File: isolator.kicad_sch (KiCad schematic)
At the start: 114 parts, among them J1 USB_C_Receptacle_USB2.0_16P, J2 USB_C_Receptacle_PowerOnly_6P, J3 USB_A, J4 USB_A, J5 USB_C_Receptacle_USB2.0_16P, J6 USB_C_Receptacle_USB2.0_16P, Q1 2N7002, T1 750313638, U1 ADuM4165, U10 TPS2553DBV, U11 TPS2553DBV, U12 TPS2553DBV, U13 TLV7041DBV, U14 TLV7041DBV, U15 NUP4202, U16 NUP4202, U17 NUP4202, U18 NUP4202, U2 NUP4202, U3 NUP4202, U4 USB2514B_Bi, U5 SN6505BDBV, U6 MIC29302WU, U7 TPS2121, U8 AP2112K-3.3, U9 TPS2553DBV, Y1 24M, Y2 24M

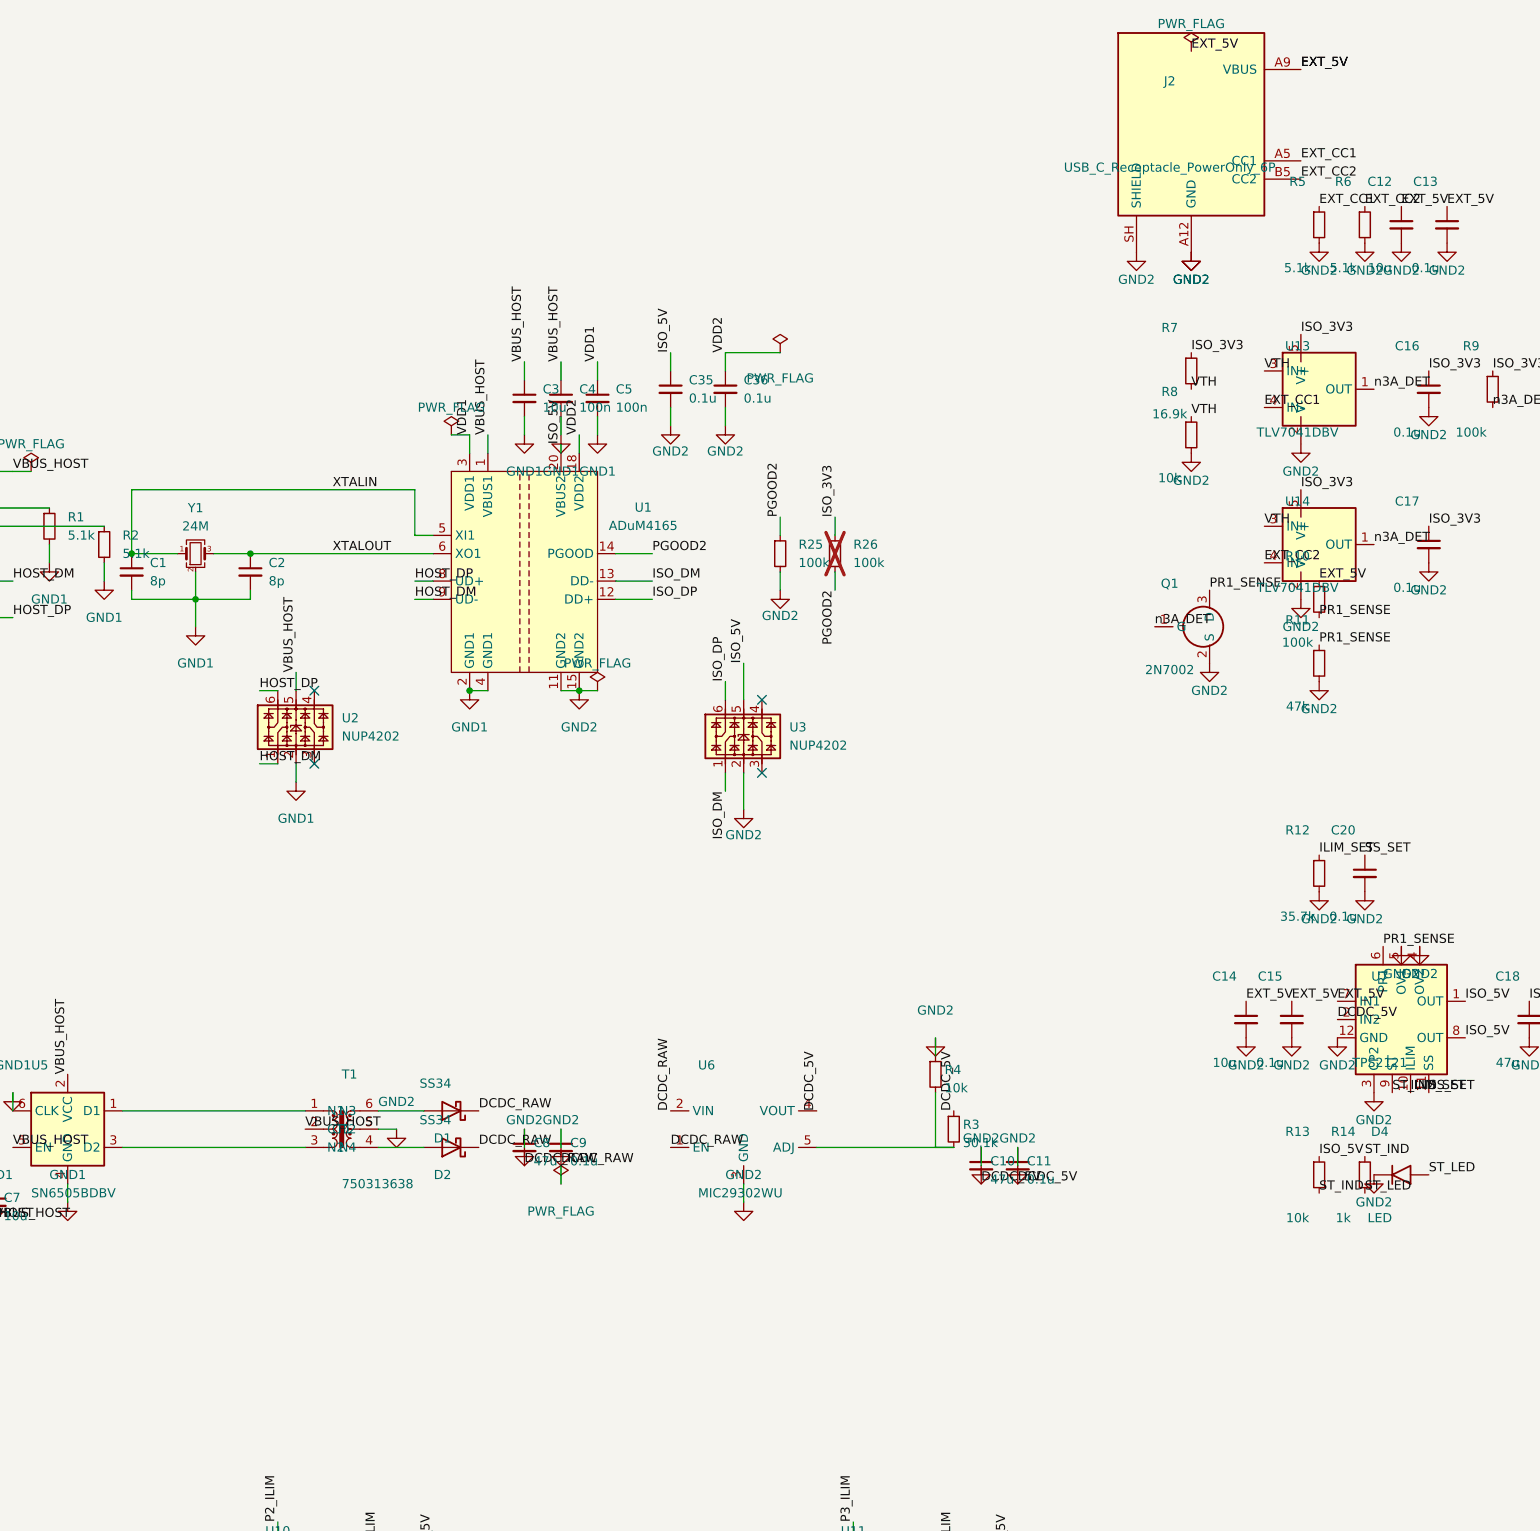
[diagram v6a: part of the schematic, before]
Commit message: feat(sch): indicators, PWR_FLAGs, stitching provision; ERC clean
Add D3 (PGOOD indicator, buffered through spare 2N7002 Q2 so the LED
never loads the shared PGOOD2 logic node) and D6 (DCDC bus-power
indicator, direct on the regulated DCDC_5V rail). Add C_stitch (1nF
2kV, DNP, in_bom no) as the sole deliberate GND1<->GND2 EMI stitching
provision besides U1, with a schematic text note. Verify the Task 4-8
PWR_FLAG sweep already covers every required rail (nothing added).
Audit no_connects: 19 total, zero stale/colliding with wires.

Reconcile lib_symbol_mismatch: fixed 5 of 11 (D_Schottky, MIC29302WU,
USB_C_Receptacle_PowerOnly_6P, LED) by restoring metadata/graphics
dropped from the cached copies vs the system library. The remaining 6
(SN6505BDBV, 2N7002 x2, TLV7041DBV x2, AP2112K-3.3, USB2514B_Bi) stay
mismatched for one-line documented reasons each: 4 are extends-vs-
flatten structural (this project's sym-lib-table only registers
isolator-lib, so caching a parent-referencing "extends" pointer would
require also caching the parent -- flattening keeps the file
self-contained, established since Task 5); 2 are the project's
intentional blank-Footprint-until-BOM-task convention (U4, U8).

ERC: 0 severity errors, exit 0. Full run: 0 errors, 7 warnings (all
justified lib_symbol_mismatch). Analyzer: ground_domains now shows
GND1 n GND2 = {U1, C_stitch}, exactly the two-domain check this task
was expected to produce.

Co-Authored-By: Claude Fable 5 <noreply@anthropic.com>
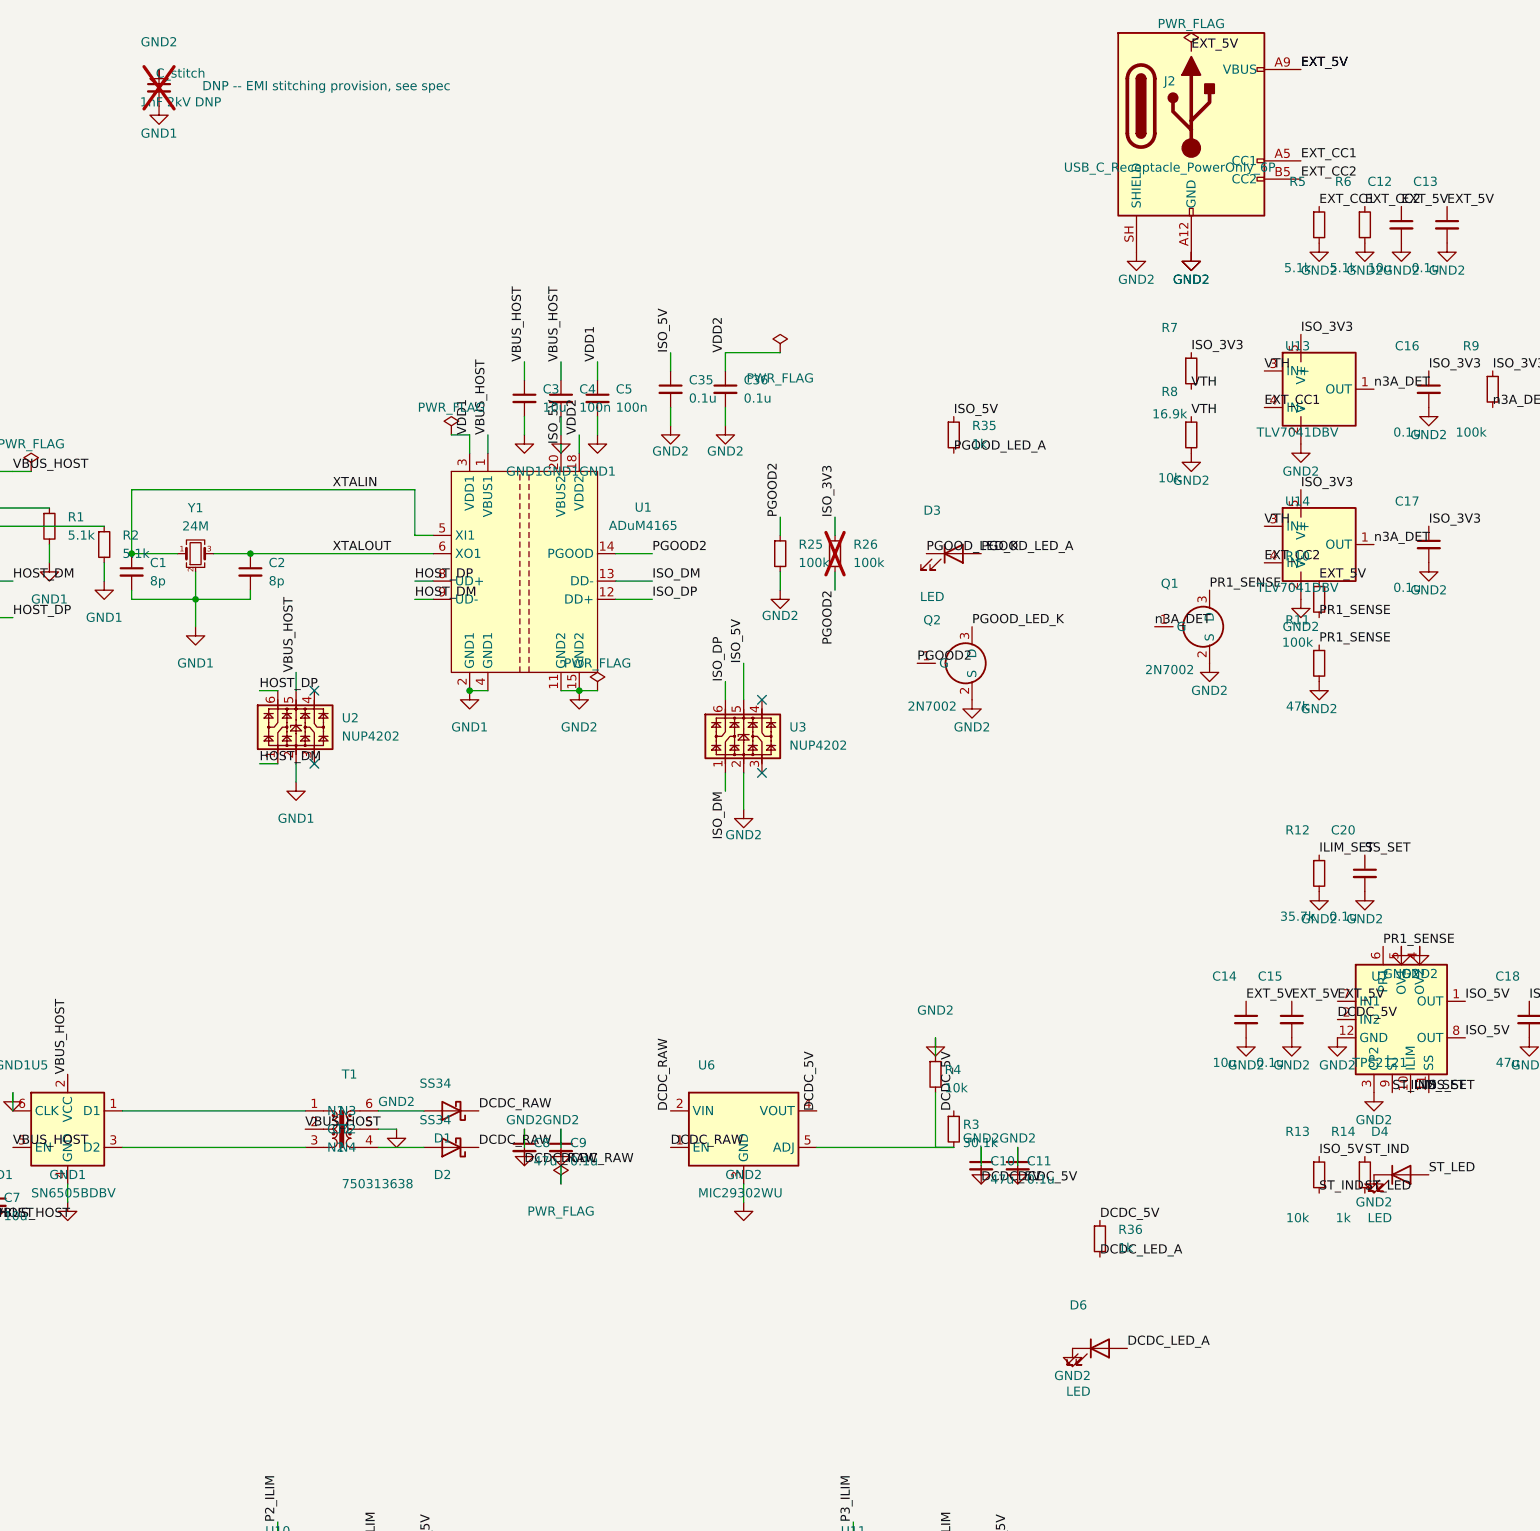
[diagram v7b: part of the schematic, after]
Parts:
- added C_stitch: 1nF 2kV DNP, symbol Device:C_Small
- added D3, D6: LED, symbol Device:LED
- added Q2: 2N7002, Package_TO_SOT_SMD:SOT-23, symbol Transistor_FET:2N7002
- added R35, R36: 1k, symbol Device:R_Small
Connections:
- net DCDC_5V: now also R36.1
- net GND1: now also C_stitch.2
- net GND2: now also C_stitch.1, D6.1 (K), Q2.2 (S)
- net ISO_5V: now also R35.1
- net PGOOD2: now also Q2.1 (G)
- new net DCDC_LED_A: D6.2 (A), R36.2
- new net PGOOD_LED_A: D3.2 (A), R35.2
- new net PGOOD_LED_K: D3.1 (K), Q2.3 (D)
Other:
- note added: "DNP -- EMI stitching provision, see spec"

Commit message: feat(sch): footprint assignment, custom RI-20-1 + WE transformer footprints
Co-Authored-By: Claude Fable 5 <noreply@anthropic.com>
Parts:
- C1, C11, C13, C15, C16, C17, C19, C2, C20, C21, C22, C23, C24, C25, C26, C27, C28, C29, C30, C31, C32, C33, C34, C35, C36, C37, C39, C4, C40, C42, C43, C45, C46, C48, C5, C6, C9: footprint (none) -> Capacitor_SMD:C_0603_1608Metric
- C10, C18, C8: footprint (none) -> Capacitor_SMD:C_1210_3225Metric
- C12, C14, C3, C38, C41, C44, C47, C7: footprint (none) -> Capacitor_SMD:C_0805_2012Metric
- C_stitch: footprint (none) -> Capacitor_SMD:C_1812_4532Metric
- D1, D2: footprint (none) -> Diode_SMD:D_SMA
- D3, D4, D6: footprint (none) -> LED_SMD:LED_0603_1608Metric
- D5: footprint (none) -> Diode_SMD:D_SOD-323
- J1, J5, J6: footprint (none) -> Connector_USB:USB_C_Receptacle_HRO_TYPE-C-31-M-12
- J2: footprint (none) -> Connector_USB:USB_C_Receptacle_GCT_USB4125-xx-x_6P_TopMnt_Horizontal
- J3, J4: footprint (none) -> Connector_USB:USB_A_Molex_67643_Horizontal
- R1, R10, R11, R12, R13, R14, R15, R16, R17, R18, R19, R2, R20, R21, R22, R23, R24, R25, R26, R27, R28, R29, R3, R30, R31, R32, R33, R34, R35, R36, R4, R5, R6, R7, R8, R9: footprint (none) -> Resistor_SMD:R_0603_1608Metric
- T1: footprint (none) -> isolator-lib:WE_750313638
- U1: footprint (none) -> isolator-lib:ADI_SOIC_IC_20_RI-20-1
- U10, U11, U12, U9: footprint (none) -> Package_TO_SOT_SMD:SOT-23-6
- U4: footprint (none) -> Package_DFN_QFN:QFN-36-1EP_6x6mm_P0.5mm_EP3.7x3.7mm
- U7: footprint (none) -> Package_DFN_QFN:Texas_VQFN-HR-12_2x2.5mm_P0.5mm
- U8: footprint (none) -> Package_TO_SOT_SMD:SOT-23-5
- Y1, Y2: footprint (none) -> Crystal:Crystal_SMD_3225-4Pin_3.2x2.5mm
